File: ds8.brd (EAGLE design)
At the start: 127 x 66 mm, 99 parts, among them IC1 TM4C1230C3PM, IC2 TPS77333, J1 9VDC, Q1 BC850, Q2 BC850, Q3 BC850, U1 LM13700M, U2 LM324, U3 LM324, U4 LM741D, X1 MAB5SH

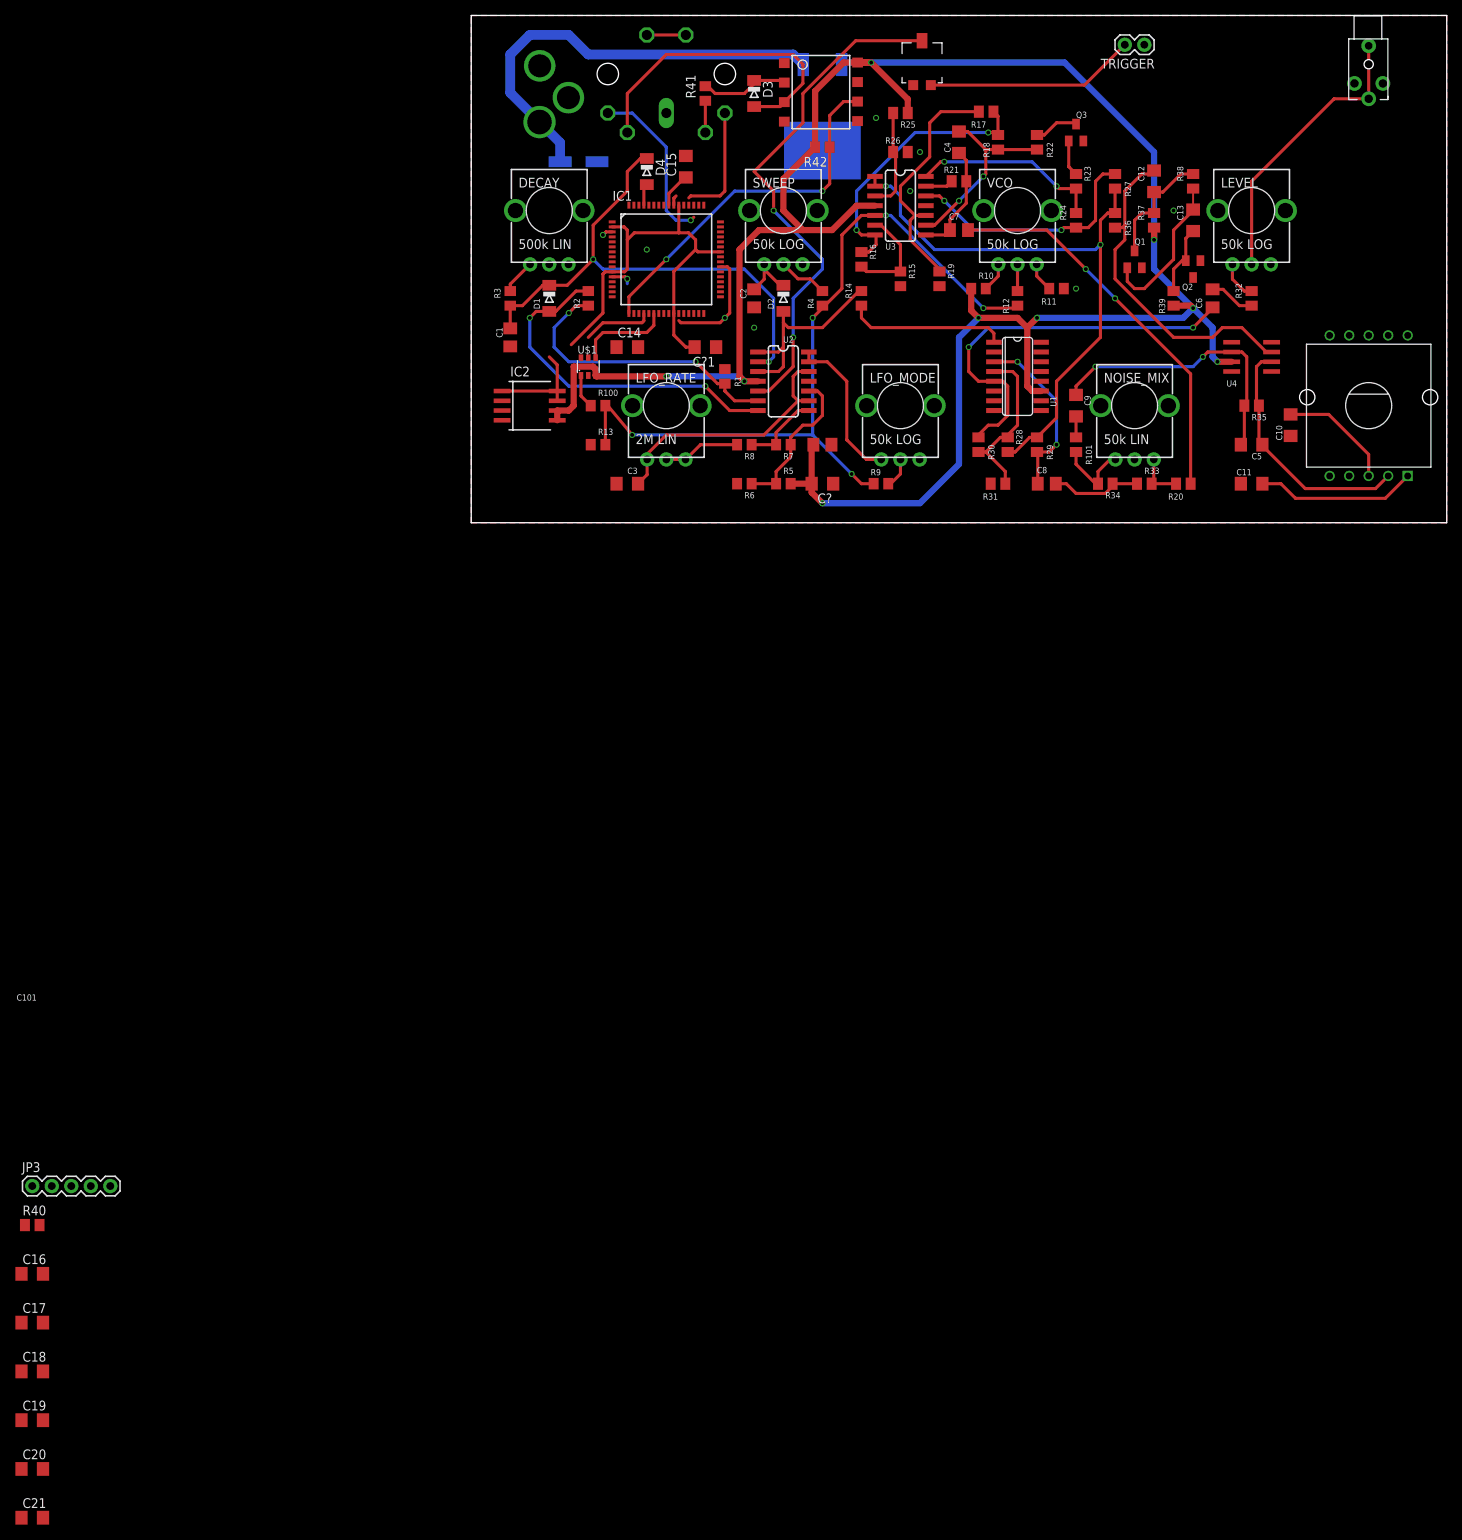
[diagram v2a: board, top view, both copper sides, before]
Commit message: TODO : Check JTAG
Don't we need to have at least a common ground for the JTAG connection ? What about using this kind of supposedly standard header ? http://www.keil.com/support/man/docs/ulinkpro/ulinkpro_hw_if_jtag10.htm
Done : board rerouted, added test points, added screw holes, moved a few things around, almost ready to be produced once we are sure about the JTAG stuff & checked the components one last time.

Signed-off-by: Kamel Makhloufi <melka@blaste.net>
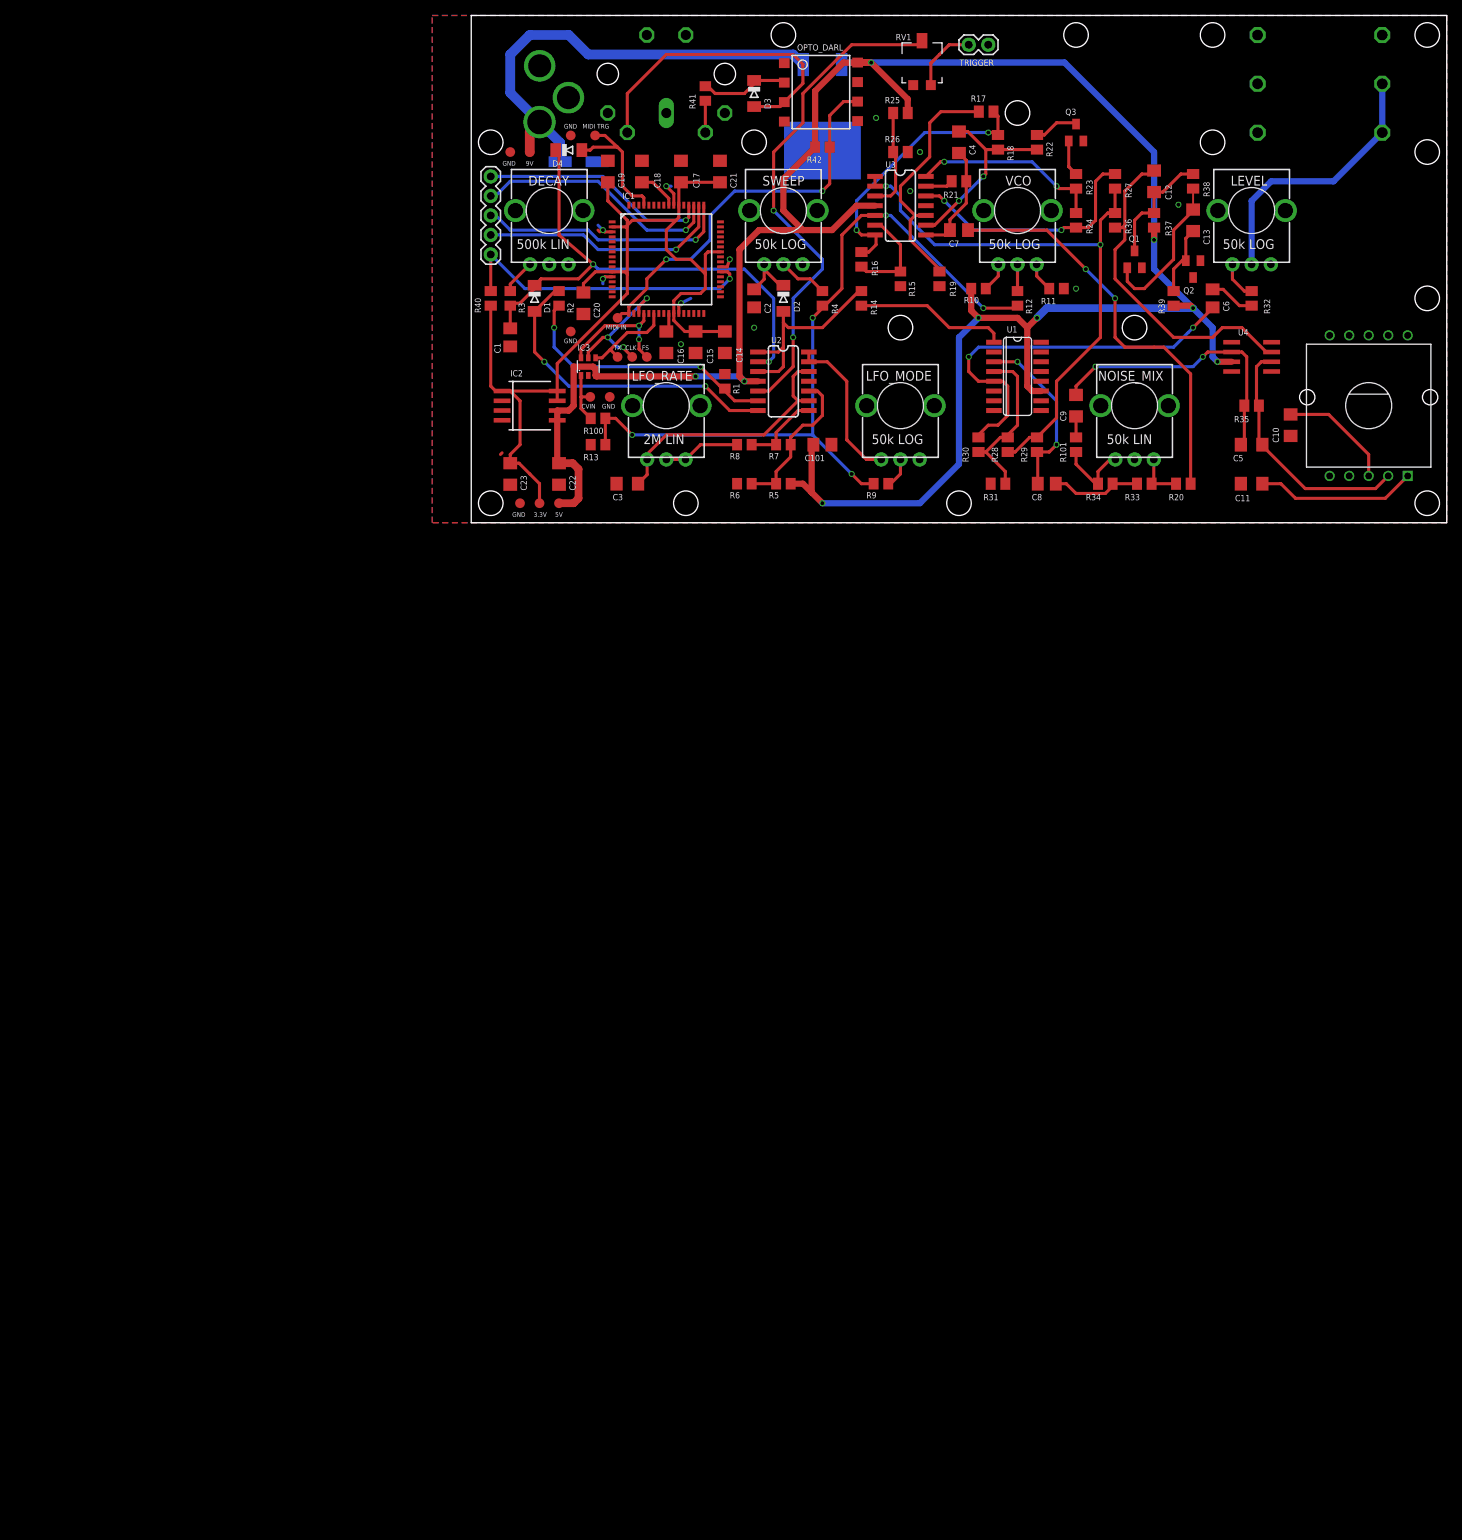
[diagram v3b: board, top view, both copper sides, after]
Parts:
- removed C?, C?1: 100n, rcl:C1206
- removed JP1: (no value), SparkFun-Connectors:STEREOJACK2.5MM_STEREOJACK2.5MM
- added C22, C23: 100n, rcl:C1206
- added IC3: DAC7512, ds8:SOT-23-6
- added TP1, TP10, TP11, TP12, TP13, TP14, TP2, TP3, TP4, TP5, TP6, TP7, TP8, TP9: TEST-POINT3X5, SparkFun-Passives:PAD.03X.05
- C15: value 3uF -> 0.01uF
- C18: value 0.01uF -> 3uF
- J1: value 9VDC -> 9VDC POSITIVE CENTER
- JP3: value (none) -> JTAG
- RV1: value TRIMPOT -> TRIGGER SENSITIVITY
- U$1: value DAC7512 -> 6.35MMJACK; device ds8:SOT-23-6 -> ds8:NMJ6HCD3
- U1: device ds8:SO16 -> ds8:DS8_SO16
- X1: value MAB5SH -> MIDI IN
- moved C21 196.8 mm to (32.4, 45.7), turned to 270 degrees
- moved C19 179.0 mm to (17.8, 45.7), turned to 270 degrees
- moved C18 175.2 mm to (22.2, 45.7), turned to 90 degrees
- moved C17 172.0 mm to (27.3, 45.7), turned to 90 degrees
- moved C20 167.9 mm to (14.6, 28.6), turned to 90 degrees
- moved C16 146.7 mm to (25.4, 23.5), turned to 90 degrees
- moved JP3 144.4 mm to (2.54, 45.1), turned to 270 degrees
- moved R40 134.6 mm to (2.54, 29.2), turned to 270 degrees
- moved U$1 105.7 mm to (110.5, 66.0), flipped to the bottom
- moved C15 22.9 mm to (29.2, 23.5)
- moved TRIGGER 20.3 mm to (67.3, 62.2)
- moved C14 12.7 mm to (33.0, 23.5), turned to 90 degrees
- moved D4 10.5 mm to (12.7, 48.5), turned to 0 degrees
- moved R2 3.81 mm to (11.4, 29.2)
- moved D1 1.90 mm to (8.26, 29.2)
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- renumbered U$2 to U100
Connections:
- net N$41 renamed RST
- removed net N$6: U$1.5
- removed net PE: X1.PE, X1.PE@
- removed net SWCLK: X1.1
- removed net SWDIO: X1.3
- net 9VDC: now also TP2.P$1
- net ARM_SSI0_CLK: now also IC3.5, TP10.P$1
- net ARM_SSI0_FS: now also IC3.6, TP11.P$1; no longer U$1.6
- net ARM_SSI0_TX: now also IC3.4, TP9.P$1; no longer U$1.4
- net CVIN: now also IC3.1, TP7.P$1; no longer U$1.1
- net GND: now also C15.1, C18.2, C22.1, C23.1, IC3.2, TP12.P$1, TP14.P$1, TP5.P$1, TP6.P$1, TP8.P$1, U$1.S, X1.PE, X1.PE@; no longer C15.2, C18.1, C?.1, C?1.1, JP1.RING1, U$1.2
- net MIDI_IN: now also TP1.P$1
- net MIDI_TRIG: now also TP13.P$1
- net N$36: now also C18.1; no longer C15.1
- net N$42: now also C16.2; no longer C21.2
- net N$57: now also U$1.R, U$1.T; no longer JP1.SHIELD, JP1.TIP
- net VCC: now also C22.2, IC3.3, TP3.P$1; no longer C?.2, U$1.3
- net VDD: now also C15.2, C21.2, C23.2, TP4.P$1; no longer C16.2, C18.2, C?1.2
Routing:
- net VDD: track 68.4 -> 129.1 mm
- net RST: track 0.00 -> 40.2 mm, vias 0 -> 1
- net TDO: track 0.00 -> 32.9 mm, vias 0 -> 1
- net TMS: track 0.00 -> 32.5 mm, vias 0 -> 1
- net TDI: track 0.00 -> 31.9 mm, vias 0 -> 1
- net TCK: track 0.00 -> 29.9 mm, vias 0 -> 1
- net SWDIO: track 22.0 -> 0.00 mm, vias 1 -> 0
- net N$34: track 27.4 -> 8.78 mm
- net ARM_SSI0_CLK: track 0.00 -> 18.0 mm, vias 0 -> 3
- net VCC: track 288.3 -> 303.9 mm
- net SWCLK: track 15.2 -> 0.00 mm
- net MIDI_TRIG: track 2.84 -> 18.0 mm
- net ARM_SSI0_FS: track 9.08 -> 16.6 mm, vias 0 -> 2
- net GND: track 19.7 -> 13.1 mm, vias 10 -> 12
- net PE: track 5.08 -> 0.00 mm
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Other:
- board text added: "3.3V"
- board text added: "5V"
- board text added: "6N138S"
- board text added: "9V"
- board text added: "AUDIO OUT"
- board text added: "CLK"
- board text added: "CVIN"
- board text added: "FS"
- board text added: "GND"
- board text added: "L7805"
- board text added: "MIDI IN"
- board text added: "MIDI TRG"
- board text added: "OPTO_DARL"
- board text added: "TX"
- board text added: "U100"
- board text added: "X2"

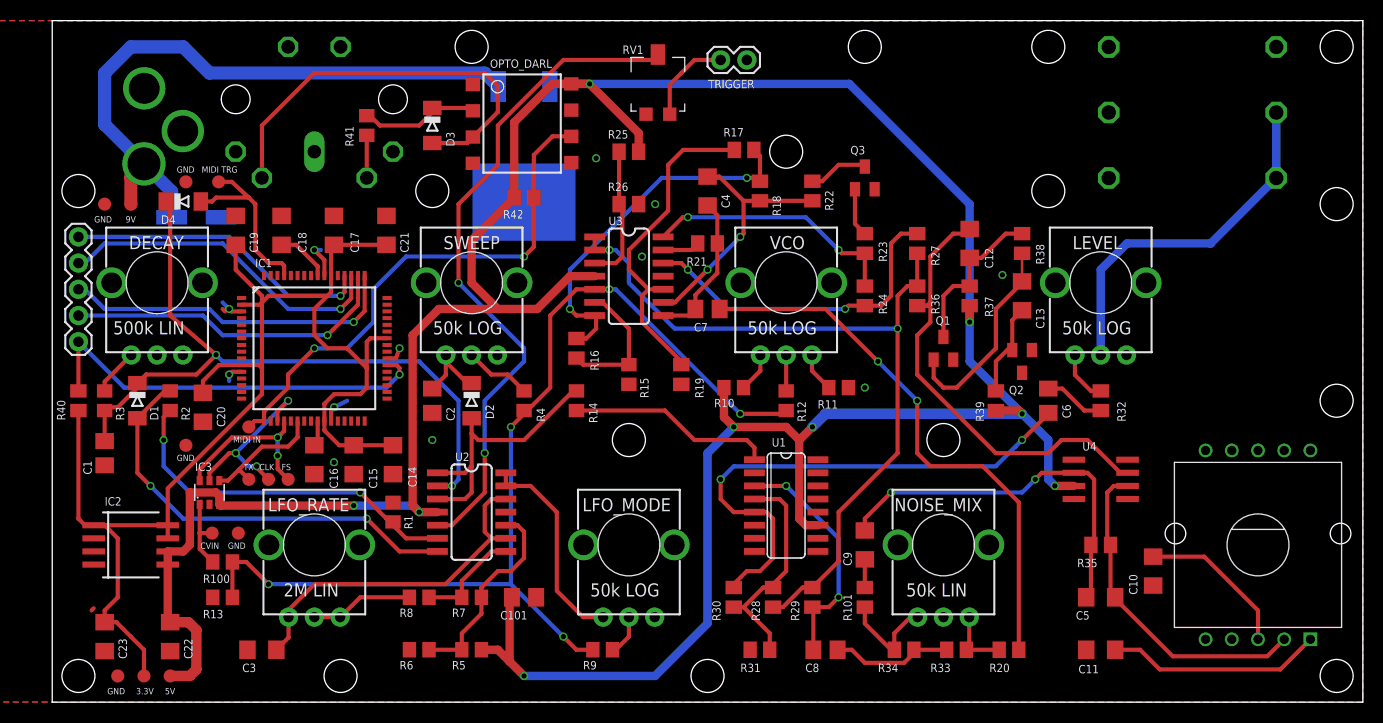
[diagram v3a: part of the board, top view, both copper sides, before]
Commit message: Mech design revisions
Moved screw holes and some little components for assembly
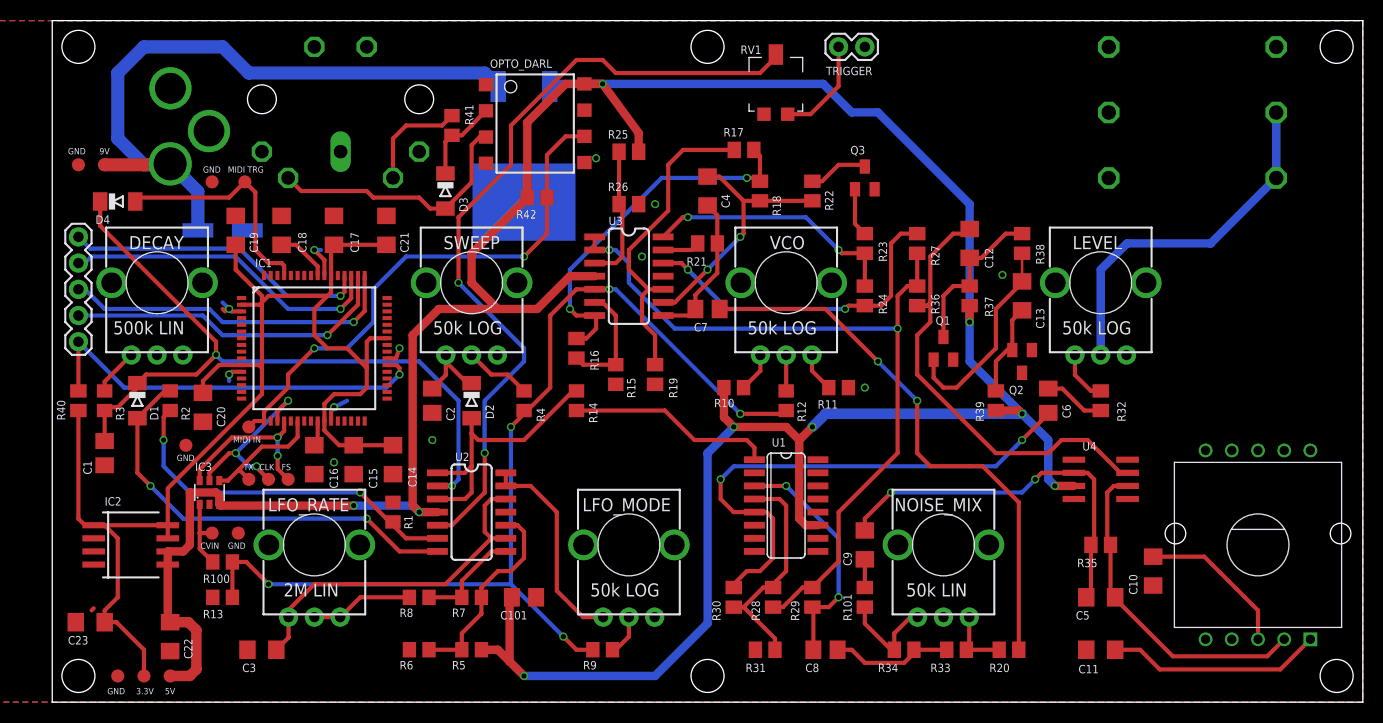
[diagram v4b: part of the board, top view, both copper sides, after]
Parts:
- moved TRIGGER 11.5 mm to (78.7, 63.5)
- moved RV1 11.4 mm to (70.1, 59.5)
- moved R41 8.25 mm to (38.7, 55.9), turned to 270 degrees
- moved D3 6.48 mm to (38.1, 49.5)
- moved D4 6.35 mm to (6.35, 48.5)
- moved TP2 4.58 mm to (5.08, 52.1)
- moved TP6 4.58 mm to (2.54, 52.1)
- moved C100 2.84 mm to (16.5, 45.7)
- moved X1 2.54 mm to (27.9, 58.4)
- moved J1 2.54 mm to (11.4, 66.0)
- moved R19 2.54 mm to (58.4, 31.8)
- moved TP13 2.54 mm to (18.7, 50.4)
- moved TP14 2.54 mm to (15.5, 50.4)
- moved C23 1.98 mm to (3.68, 7.75), turned to 0 degrees
- moved R15 1.27 mm to (54.6, 31.8)
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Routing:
- net N$35: track 40.7 -> 25.4 mm
- net TRIGGER: track 65.6 -> 77.5 mm
- net N$18: track 4.13 -> 10.4 mm
- net MIDI_TRIG: track 18.0 -> 23.0 mm
- net 9VDC: track 61.9 -> 66.2 mm
- net N$26: track 11.7 -> 8.26 mm
- net N$3: track 68.6 -> 71.0 mm
- net N$7: track 13.2 -> 11.4 mm
- net N$34: track 8.78 -> 9.86 mm
- net TMS: track 32.5 -> 31.4 mm
- net N$10: track 32.0 -> 30.9 mm
- net MIDI_IN: track 51.3 -> 51.8 mm
